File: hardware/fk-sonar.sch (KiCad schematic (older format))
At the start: 81 parts, among them J1 Conn_01x03, J2 CONN-HDR-2x5, J3 RF-SMA-EDGE, J4 MICRO-USB, J5 S2B-PH-SM4-TB, J6 Conn_01x04, J7 S2B-PH-SM4-TB, J8 Conn_01x03, J9 Conn_01x05, M1 MOUNT_HOLE, M2 FIDUCIAL, M3 MOUNT_HOLE, M4 MOUNT_HOLE, M5 FIDUCIAL, M6 MOUNT_HOLE, Q1 2N7002LT1G, Q2 2N7002LT1G, Q3 2N7002LT1G, Q4 2N7002LT1G, SW1 SPNO, U1 ATSAMD21G18A-AU, U2 RFM95W, U3 BQ24074RGTT, U4 S25FL116K0XMFI041, U5 MAX1704XX, U6 MCP1700T-3302E/MB, Y1 FC-135

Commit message: Upgrade to Kicad 5. Also adding SK6812 and molex connectors.
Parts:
- removed D2: Orange, RocketScreamKicadLibrary:LED-0603, symbol LED-SINGLE
- removed D3: Yellow, RocketScreamKicadLibrary:LED-0603, symbol LED-SINGLE
- removed D4: Blue, RocketScreamKicadLibrary:LED-0603, symbol LED-SINGLE
- removed J2: CONN-HDR-2x5, conservify:HDR_2x5_Pitch1.27mm_SMD_JTAG_SWD, symbol CONN-HDR-2x5
- removed J8: Conn_01x03, conservify:Molex_CLIK-Mate_502382-0370_1x03_P1.25mm_Vertical, symbol Conn_01x03
- removed Q2, Q3, Q4: 2N7002LT1G, RocketScreamKicadLibrary:SOT-23, symbol MOSFET-N
- removed R4, R5, R6: 2K2, RocketScreamKicadLibrary:RES-0603, symbol RESISTOR
- added J2: CONN_02x05_SWD, conservify:HDR_02x05_Pitch1.27mm_SMD_SWD, symbol conservify:CONN_02x05_SWD
- added J8: CONN_01x03_SERIAL, conservify:Molex_CLIK-Mate_502382-0370_1x03_P1.25mm_Vertical, symbol conservify:CONN_01x03_SERIAL
- added U7: SK6812, conservify:SK6812, symbol conservify:SK6812
- C1, C10, C11, C12, C13, C14, C15, C16, C17, C18, C19, C2, C20, C21, C3, C4, C5, C6, C7, C8, C9: footprint RocketScreamKicadLibrary:CAP-0603 -> conservify:CAP-0603; symbol CAPACITOR-CERAMIC -> fk-sonar-rescue:CAPACITOR-CERAMIC
- D1, D7, D8: footprint RocketScreamKicadLibrary:LED-0603 -> conservify:LED-0603; symbol LED-SINGLE -> fk-sonar-rescue:LED-SINGLE
- D5: footprint RocketScreamKicadLibrary:SOT-1016 -> conservify:SOT-1016; symbol DIODE_DUAL_Schottky -> fk-sonar-rescue:DIODE_DUAL_Schottky
- D6: footprint RocketScreamKicadLibrary:SOT-143B -> conservify:SOT-143B; symbol PRTR5V0U2X -> conservify:PRTR5V0U2X
- F1: footprint RocketScreamKicadLibrary:MF-PSMF020X -> conservify:MF-PSMF020X; symbol FUSE -> conservify:FUSE
- J1: footprint Socket_Strips:Socket_Strip_Straight_1x03_Pitch2.54mm -> conservify:Molex_CLIK-Mate_502382-0370_1x03_P1.25mm_Vertical; symbol Conn_01x03 -> fk-sonar-rescue:Conn_01x03
- J3: footprint RocketScreamKicadLibrary:RF-SMA-EDGE -> conservify:RF-SMA-EDGE; symbol RF-SMA-EDGE -> fk-sonar-rescue:RF-SMA-EDGE
- J4: footprint RocketScreamKicadLibrary:MICRO-USB -> conservify:MICRO-USB; symbol MICRO-USB -> fk-sonar-rescue:MICRO-USB
- J5, J7: footprint RocketScreamKicadLibrary:S2B-PH-SM4-TB -> conservify:S2B-PH-SM4-TB; symbol S2B-PH-SM4-TB -> fk-sonar-rescue:S2B-PH-SM4-TB
- J6: footprint Socket_Strips:Socket_Strip_Straight_1x04_Pitch2.54mm -> conservify:Molex_CLIK-Mate_502382-0470_1x04_P1.25mm_Vertical; symbol Conn_01x04 -> fk-sonar-rescue:Conn_01x04
- J9: footprint conservify:Molex_CLIK-Mate_502386-0570_1x05_P1.25mm_Horizontal -> conservify:Molex_CLIK-Mate_502382-0570_1x05_P1.25mm_Vertical; symbol Conn_01x05 -> fk-sonar-rescue:Conn_01x05
- L1, L2: footprint RocketScreamKicadLibrary:IND-0603 -> conservify:IND-0603; symbol INDUCTOR -> conservify:INDUCTOR
- M1, M3, M4, M6: footprint RocketScreamKicadLibrary:HOLE_NPTH_2.2MM -> conservify:HOLE_NPTH_2.54MM; symbol MOUNT_HOLE -> conservify:MOUNT_HOLE
- M2, M5: footprint RocketScreamKicadLibrary:FIDUCIAL-1MM -> conservify:FIDUCIAL-1MM; symbol FIDUCIAL -> conservify:FIDUCIAL
- Q1: footprint RocketScreamKicadLibrary:SOT-23 -> conservify:SOT-23; symbol MOSFET-N -> fk-sonar-rescue:MOSFET-N
- R1, R10, R11, R12, R13, R14, R15, R16, R17, R18, R19, R2, R20, R21, R22, R3, R7, R8, R9: footprint RocketScreamKicadLibrary:RES-0603 -> conservify:RES-0603; symbol RESISTOR -> conservify:RESISTOR
- SW1: symbol TACT-SWITCH_2Pins -> fk-sonar-rescue:TACT-SWITCH_2Pins
- U1: footprint RocketScreamKicadLibrary:TQFP-48_7x7mm_Pitch0.5mm -> conservify:TQFP-48_7x7mm_Pitch0.5mm; symbol ATSAMD21G18A-AU -> fk-sonar-rescue:ATSAMD21G18A-AU
- U2: footprint RocketScreamKicadLibrary:RFM9xW -> conservify:RFM9xW; symbol RFM9xW -> conservify:RFM9xW
- U3: footprint RocketScreamKicadLibrary:QFN-16_3x3mm -> conservify:QFN-16_3x3mm; symbol BQ24074 -> conservify:BQ24074
- U4: footprint RocketScreamKicadLibrary:SOIC-8-N -> conservify:SOIC-8-N; symbol S25FL1xxK0XM -> conservify:S25FL1xxK0XM
- U5: footprint Housings_DFN_QFN:DFN-8-1EP_3x2mm_Pitch0.5mm -> conservify:DFN-8-1EP_3x2mm_Pitch0.5mm; symbol MAX1704XX -> conservify:MAX1704XX
- U6: footprint RocketScreamKicadLibrary:SOT-89 -> conservify:SOT-89; symbol MCP1700T-XXX2E -> conservify:MCP1700T-XXX2E
- Y1: footprint RocketScreamKicadLibrary:ABS07 -> conservify:ABS07; symbol CRYSTAL -> conservify:CRYSTAL
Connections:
- wire segments 298 -> 338
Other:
- note removed: "LED"
- moved on the sheet: C17, C18, D1, J6, Q1, R1, R19, R20, R21, R22, U5

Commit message: Schematic layout.
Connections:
- no-connect marks 20 -> 19
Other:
- note added: "FUEL GAUGE"
- note removed: "SWD/JTAG"
- moved on the sheet: C17, C18, D1, M1, M2, M3, M4, M5, M6, Q1, R1, R19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

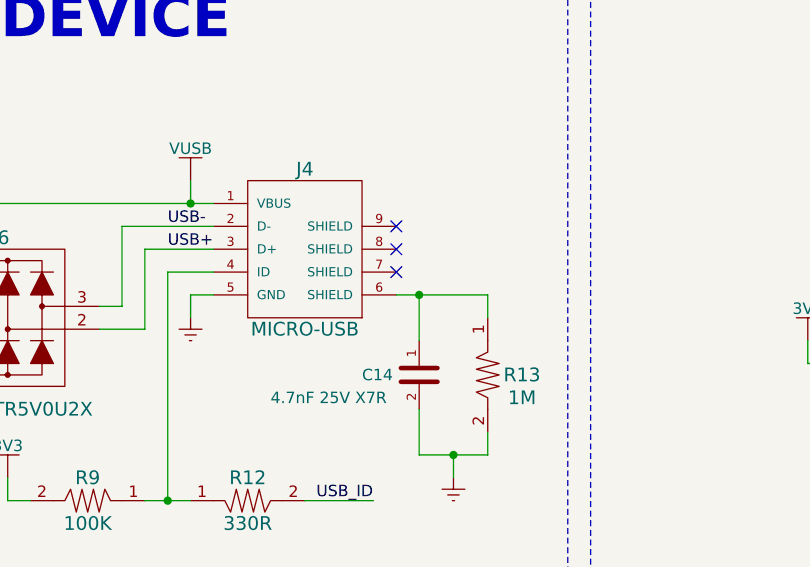
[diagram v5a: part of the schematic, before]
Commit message: New USB for vertical entry.
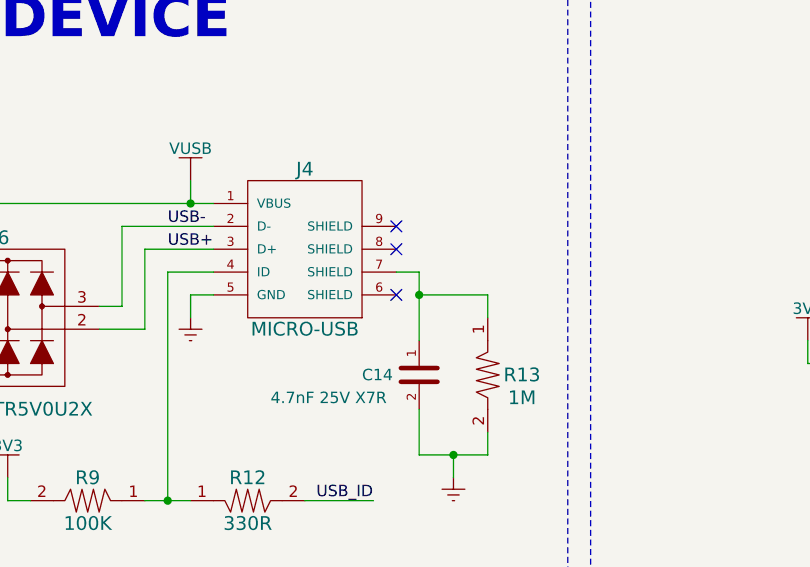
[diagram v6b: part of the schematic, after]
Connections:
- wire segments 338 -> 339
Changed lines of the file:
@@
 	9900 6550 9900 7550
-Wire Wire Line
-	10900 6650 11000 6650
 Wire Wire Line
 	11000 7150 11000 7350
@@
 Connection ~ 2050 10050
 Connection ~ 2050 9850
-Connection ~ 11000 6650
 Connection ~ 7450 6250
 Connection ~ 9900 7550
@@
 NoConn ~ 10900 6350
 NoConn ~ 10900 6450
-NoConn ~ 10900 6550
 NoConn ~ 6350 7750
 NoConn ~ 5900 7750
@@
 Text Notes 2000 5550 0    180  ~ 36
 FUEL GAUGE
+Wire Wire Line
+	10900 6550 11000 6550
+Wire Wire Line
+	11000 6550 11000 6650
+Connection ~ 11000 6650
+NoConn ~ 10900 6650
 $EndSCHEMATC

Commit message: Consistent part values across our schematics.
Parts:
- C1, C10, C15, C16: value 4.7uF 10V X5R -> 4.7uF
- C11: value 1uF 50V X5R -> 1uF
- C12: value 47uF 10V X5R -> 47uF
- C14: value 4.7nF 25V X7R -> 4.7nF
- C17, C19, C21, C6: value 1uF 10V X5R -> 1uF
- R19: value 1k -> 1K

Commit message: Part updates.
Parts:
- C1, C10, C12, C15, C16: Critical (none) -> (none); MFN (none) -> AVX; MFP (none) -> 0603ZD475MAT2A; Notes (none) -> (none); Package (none) -> (none); Source (none) -> ANY; Subsystem (none) -> (none)
- C11: Critical (none) -> (none); MFN (none) -> Taiyo Yuden; MFP (none) -> UMK107BJ105KA-T; Notes (none) -> (none); Package (none) -> (none); Source (none) -> ANY; Subsystem (none) -> (none)
- C13, C2, C20, C5, C7, C8, C9: Critical (none) -> (none); MFN (none) -> Murata Electronics; MFP (none) -> GRM188R71H104KA93D; Notes (none) -> (none); Package (none) -> (none); Source (none) -> ANY; Subsystem (none) -> (none)
- C14: Critical (none) -> (none); MFN (none) -> KEMET; MFP (none) -> C0603C472K9RACTU; Notes (none) -> (none); Package (none) -> (none); Source (none) -> ANY; Subsystem (none) -> (none); spn1 603-AC603KRX7R8BB472 -> 80-C0603C472K9R
- C17, C19, C21, C6: Critical (none) -> (none); MFN (none) -> Taiyo Yuden; MFP (none) -> UMK107BJ105KA-T; Notes (none) -> (none); Package (none) -> (none); Source (none) -> ANY; Subsystem (none) -> (none); spn1 581-0603YD105K -> 963-UMK107BJ105KA-T
- C18: Critical (none) -> (none); MFN (none) -> AVX; MFP (none) -> 0603YC103K4T2A; Notes (none) -> (none); Package (none) -> (none); Source (none) -> ANY; Subsystem (none) -> (none)
- C3, C4: Critical (none) -> (none); MFN (none) -> AVX; MFP (none) -> 06035A180JAT2A; Notes (none) -> (none); Package (none) -> (none); Source (none) -> ANY; Subsystem (none) -> (none)
- D1: Critical (none) -> (none); MFN (none) -> Lite-On; MFP (none) -> LTST-C190KFKT; Notes (none) -> (none); Package (none) -> (none); Source (none) -> ANY; Subsystem (none) -> (none)
- D5: Critical (none) -> (none); MFN (none) -> Nexperia; MFP (none) -> PMEG3020CPA,115; Notes (none) -> (none); Package (none) -> (none); Source (none) -> ANY; Subsystem (none) -> (none)
- D6: Critical (none) -> (none); MFN (none) -> Nexperia; MFP (none) -> PRTR5V0U2X,215; Notes (none) -> (none); Package (none) -> (none); Source (none) -> ANY; Subsystem (none) -> (none)
- D7: Critical (none) -> (none); MFN (none) -> Lite-On; MFP (none) -> LTST-C190KGKT; Notes (none) -> (none); Package (none) -> (none); Source (none) -> ANY; Subsystem (none) -> (none)
- D8: Critical (none) -> (none); MFN (none) -> Lite-On; MFP (none) -> LTST-C190KRKT; Notes (none) -> (none); Package (none) -> (none); Source (none) -> ANY; Subsystem (none) -> (none)
- F1: Critical (none) -> (none); MFN (none) -> Bourns; MFP (none) -> MF-PSMF050X-2; Notes (none) -> (none); Package (none) -> (none); Source (none) -> ANY; Subsystem (none) -> (none)
- J1, J8: Critical (none) -> (none); MFN (none) -> Molex; MFP (none) -> 502382-0370; Notes (none) -> (none); Package (none) -> (none); SPN1 (none) -> 538-502382-0370; Source (none) -> ANY; Subsystem (none) -> (none); Supplier1 (none) -> mouser
- J2: Critical (none) -> (none); MFN (none) -> Amphenol FCI; MFP (none) -> 20021121-00010C4LF; Notes (none) -> (none); Package (none) -> (none); SPN1 (none) -> 649-202112100010C4LF; Source (none) -> ANY; Subsystem (none) -> (none); Supplier1 (none) -> mouser
- J3: Critical (none) -> (none); MFN (none) -> (none); MFP (none) -> S01-SJEDM-11BS05; Notes (none) -> (none); Package (none) -> (none); Source (none) -> ANY; Subsystem (none) -> (none)
- J4: Critical (none) -> (none); MFN (none) -> Hirose Connector; MFP (none) -> ZX62D-B-5PA8(30); Notes (none) -> (none); Package (none) -> (none); Source (none) -> ANY; Subsystem (none) -> (none)
- J5, J7: Critical (none) -> (none); MFN (none) -> JST; MFP (none) -> S2B-PH-SM4-TB(LF)(SN); Notes (none) -> (none); Package (none) -> (none); Source (none) -> ANY; Subsystem (none) -> (none)
- J6: value Conn_01x04 -> CONN_01x04; Critical (none) -> (none); MFN (none) -> (none); MFP (none) -> (none); Notes (none) -> (none); Package (none) -> (none); SPN1 (none) -> (none); Source (none) -> ANY; Subsystem (none) -> (none); Supplier1 (none) -> (none)
- J9: Critical (none) -> (none); MFN (none) -> Molex; MFP (none) -> 502382-0570; Notes (none) -> (none); Package (none) -> (none); SPN1 (none) -> 538-502382-0570; Source (none) -> ANY; Subsystem (none) -> (none); Supplier1 (none) -> mouser
- L1, L2: value BKP1005TS121-T -> BLM18KG221SN1D; Critical (none) -> (none); MFN (none) -> Murata Electronics; MFP (none) -> BLM18KG221SN1D; Notes (none) -> (none); Package (none) -> (none); Source (none) -> ANY; Subsystem (none) -> (none); spn1 963-BKP1608HS121-T -> 81-BLM18KG221SN1D
- M1, M2, M3, M4, M5, M6: Critical (none) -> (none); MFN (none) -> (none); MFP (none) -> (none); Notes (none) -> (none); Package (none) -> (none); SPN1 (none) -> (none); Source (none) -> ANY; Subsystem (none) -> (none); Supplier1 (none) -> (none)
- Q1: Critical (none) -> (none); MFN (none) -> ON Semiconductor; MFP (none) -> 2N7002LT1G; Notes (none) -> (none); Package (none) -> (none); Source (none) -> ANY; Subsystem (none) -> (none)
- R1, R11, R17: Critical (none) -> (none); MFN (none) -> Yageo; MFP (none) -> RC0603FR-072K2L; Notes (none) -> (none); Package (none) -> (none); Source (none) -> ANY; Subsystem (none) -> (none)
- R10: Critical (none) -> (none); MFN (none) -> Panasonic; MFP (none) -> ERJ-S03F2941V; Notes (none) -> (none); Package (none) -> (none); Source (none) -> ANY; Subsystem (none) -> (none)
- R12, R3: Critical (none) -> (none); MFN (none) -> Yageo; MFP (none) -> RC0603FR-07330RL; Notes (none) -> (none); Package (none) -> (none); Source (none) -> ANY; Subsystem (none) -> (none)
- R13: Critical (none) -> (none); MFN (none) -> Yageo; MFP (none) -> RC0603FR-071ML; Notes (none) -> (none); Package (none) -> (none); Source (none) -> ANY; Subsystem (none) -> (none)
- R14, R15, R21, R22: Critical (none) -> (none); MFN (none) -> Yageo; MFP (none) -> AF0603JR-074K7L; Notes (none) -> (none); Package (none) -> (none); Source (none) -> ANY; Subsystem (none) -> (none)
- R16, R18, R2: Critical (none) -> (none); MFN (none) -> Yageo; MFP (none) -> RC0603FR-0710KL; Notes (none) -> (none); Package (none) -> (none); Source (none) -> ANY; Subsystem (none) -> (none)
- R19: Critical (none) -> (none); MFN (none) -> (none); MFP (none) -> (none); Notes (none) -> (none); Package (none) -> (none); Source (none) -> ANY; Subsystem (none) -> (none); spn1 603-RC0603FR-071KL -> 603-RC0603FR-07330RL
- R20: Critical (none) -> (none); MFN (none) -> Yageo; MFP (none) -> RC0603FR-07180RL; Notes (none) -> (none); Package (none) -> (none); Source (none) -> ANY; Subsystem (none) -> (none)
- R7: Critical (none) -> (none); MFN (none) -> Panasonic; MFP (none) -> ERJ-PA3F1181V; Notes (none) -> (none); Package (none) -> (none); Source (none) -> ANY; Subsystem (none) -> (none)
- R8: Critical (none) -> (none); MFN (none) -> Panasonic Industrial Devices; MFP (none) -> ERJ-3EKF4642V; Notes (none) -> (none); Package (none) -> (none); Source (none) -> ANY; Subsystem (none) -> (none)
- R9: Critical (none) -> (none); MFN (none) -> Yageo; MFP (none) -> RC0603FR-07100KL; Notes (none) -> (none); Package (none) -> (none); Source (none) -> ANY; Subsystem (none) -> (none)
- SW1: Critical (none) -> (none); MFN (none) -> Wurth Electronics; MFP (none) -> 434331045822; Notes (none) -> (none); Package (none) -> (none); Source (none) -> ANY; Subsystem (none) -> (none)
- U1: Critical (none) -> (none); MFN (none) -> Microchip Technology / Atmel; MFP (none) -> ATSAMD21G18A-AU; Notes (none) -> (none); Package (none) -> (none); Source (none) -> ANY; Subsystem (none) -> (none)
- U2: Critical (none) -> (none); MFN (none) -> (none); MFP (none) -> (none); Notes (none) -> (none); Package (none) -> (none); SPN1 (none) -> (none); Source (none) -> ANY; Subsystem (none) -> (none)
- U3: Critical (none) -> (none); MFN (none) -> Texas Instruments; MFP (none) -> BQ24074RGTT; Notes (none) -> (none); Package (none) -> (none); Source (none) -> ANY; Subsystem (none) -> (none)
- U4: Critical (none) -> (none); MFN (none) -> Cypress Semiconductor; MFP (none) -> S25FL116K0XMFI041; Notes (none) -> (none); Package (none) -> (none); Source (none) -> ANY; Subsystem (none) -> (none)
- U5: Critical (none) -> (none); MFN (none) -> Maxim Integrated; MFP (none) -> MAX17043G+U; Notes (none) -> (none); Package (none) -> (none); Source (none) -> ANY; Subsystem (none) -> (none)
- U6: Critical (none) -> (none); MFN (none) -> Microchip Technology; MFP (none) -> MCP1700T-3302E/MB; Notes (none) -> (none); Package (none) -> (none); Source (none) -> ANY; Subsystem (none) -> (none)
- U7: Critical (none) -> (none); MFN (none) -> Adafruit; MFP (none) -> 1655; Notes (none) -> (none); Package (none) -> (none); SPN1 (none) -> 1528-1104-ND; Source (none) -> ANY; Subsystem (none) -> (none); Supplier1 (none) -> digikey
- Y1: Critical (none) -> (none); MFN (none) -> Epson Timing; MFP (none) -> FC-135 32.7680KA-A3; Notes (none) -> (none); Package (none) -> (none); Source (none) -> ANY; Subsystem (none) -> (none)
